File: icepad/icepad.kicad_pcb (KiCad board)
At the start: 2 copper layers, 50 parts, among them U1 STM32F042K6Tx, U2 TPD2EUSB30A, U3 IES0105S03

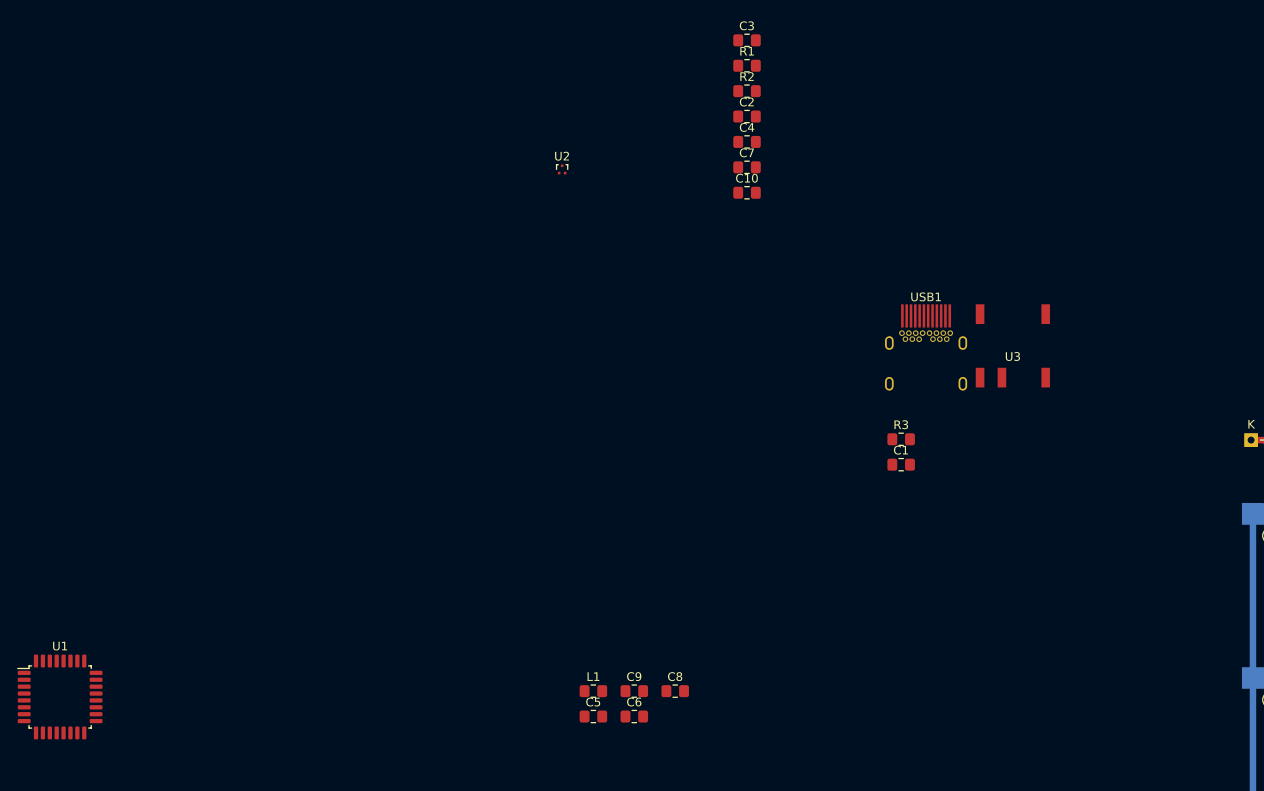
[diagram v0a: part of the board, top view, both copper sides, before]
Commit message: routed MCU and connector
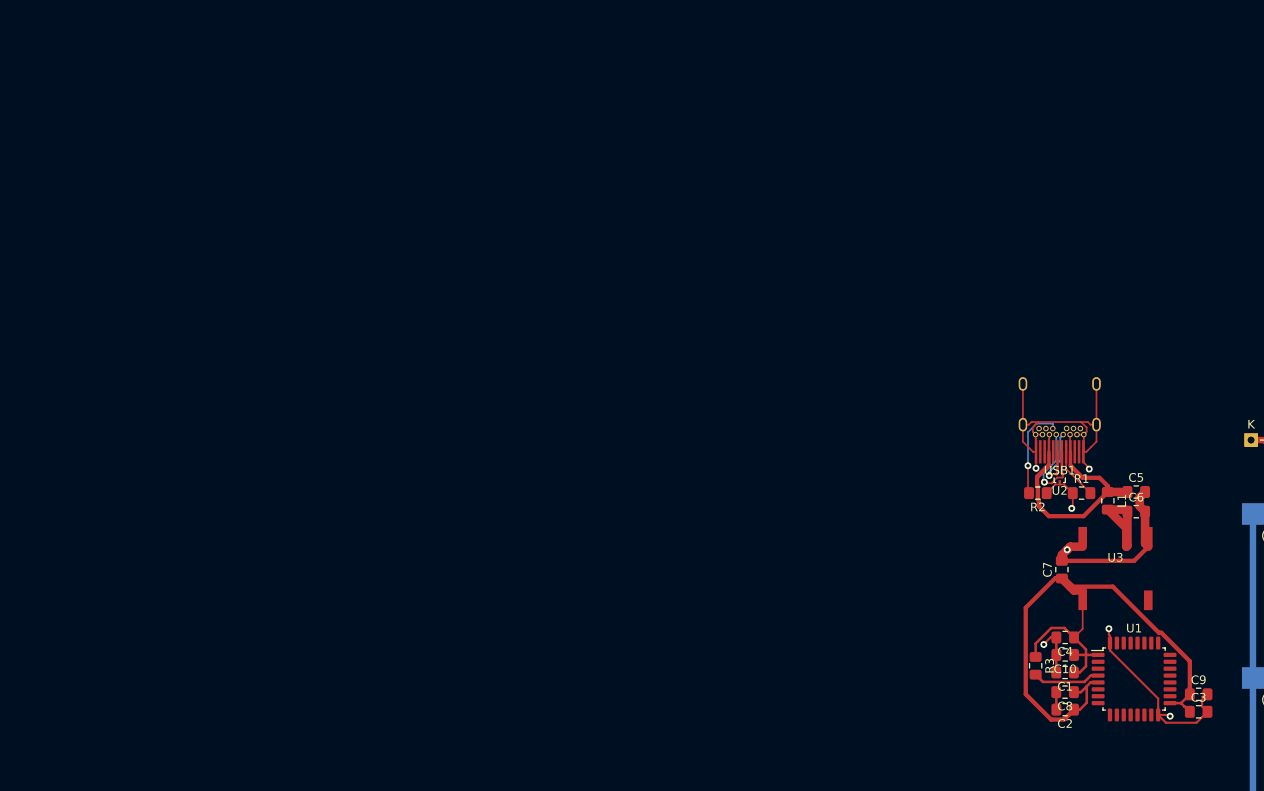
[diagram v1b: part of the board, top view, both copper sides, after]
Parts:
- moved U1 124.7 mm to (155.3, 89.7)
- moved C3 94.0 mm to (162.8, 93.5)
- moved C2 78.2 mm to (147.3, 93.2), turned to 180 degrees
- moved C4 68.4 mm to (147.3, 84.8), turned to 180 degrees
- moved C5 68.2 mm to (155.6, 67.9)
- moved U2 68.0 mm to (146.7, 66.3), turned to 180 degrees
- moved C9 65.5 mm to (162.8, 91.4)
- moved C10 65.2 mm to (147.3, 86.9), turned to 180 degrees
- moved L1 63.7 mm to (152.3, 69.0), turned to 270 degrees
- moved R1 63.0 mm to (149.2, 68.1)
- moved C6 63.0 mm to (155.6, 70.2)
- moved C7 59.3 mm to (146.9, 77.0), turned to 90 degrees
- moved R2 57.6 mm to (144.1, 68.1), turned to 180 degrees
- moved C8 45.3 mm to (147.3, 91.2), turned to 180 degrees
- moved C1 30.7 mm to (147.3, 88.9), turned to 180 degrees
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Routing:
- net GND: track 0.00 -> 98.0 mm, vias 0 -> 7
- net +3V3: track 0.00 -> 79.9 mm
- net VBUS: track 0.00 -> 30.6 mm
- net DP: track 0.00 -> 11.9 mm, vias 0 -> 1
- net Net-(C6-Pad1): track 0.00 -> 11.7 mm
- net Net-(R2-Pad2): track 0.00 -> 11.0 mm, vias 0 -> 1
- net DN: track 0.00 -> 9.05 mm, vias 0 -> 1
- net Net-(R3-Pad2): track 0.00 -> 7.91 mm
- net Net-(R1-Pad2): track 0.00 -> 5.97 mm
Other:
- net class Default: clearance 0.25 -> 0.2; trace_width 0.75 -> 0.5
- net class Key Matrix added: clearance 0.2, trace_width 0.75, via_dia 0.8, via_drill 0.4
- rule trace_clearance: 0.25 -> 0.2

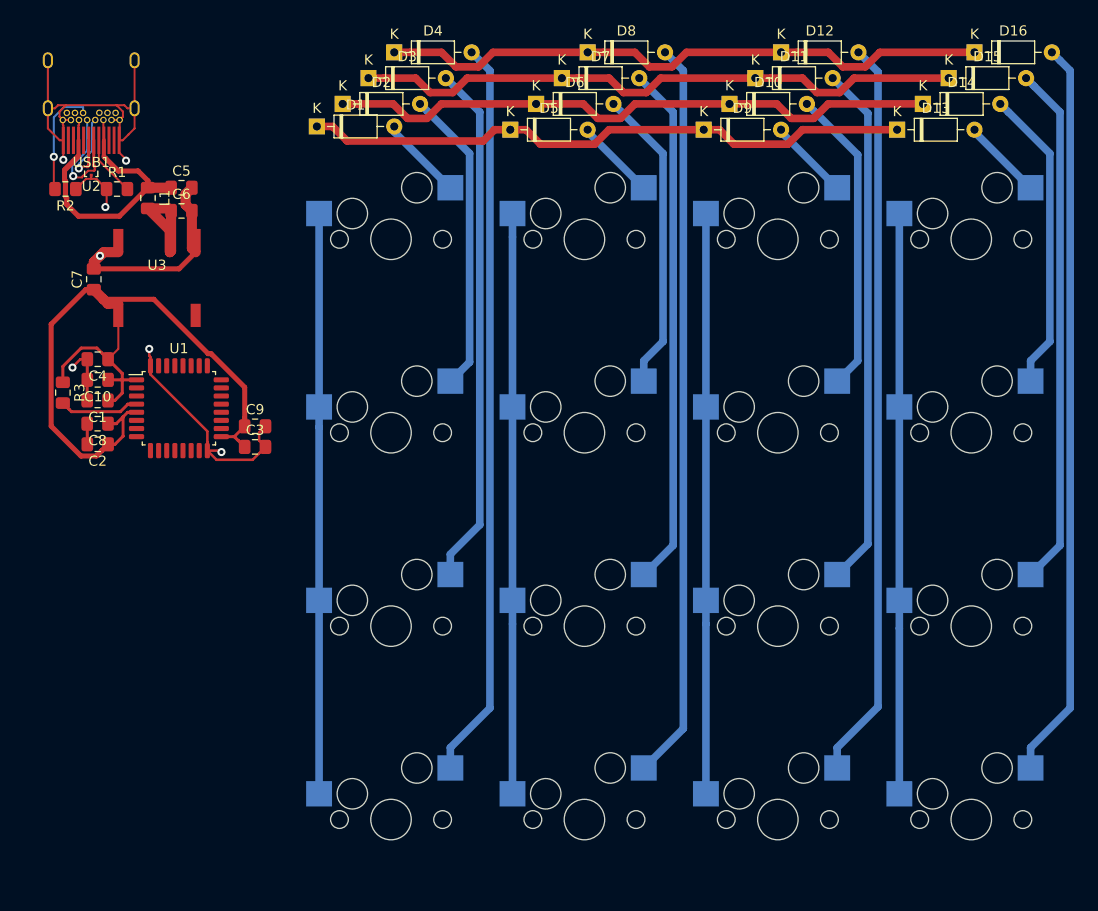
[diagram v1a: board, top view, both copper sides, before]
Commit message: completed routing without led
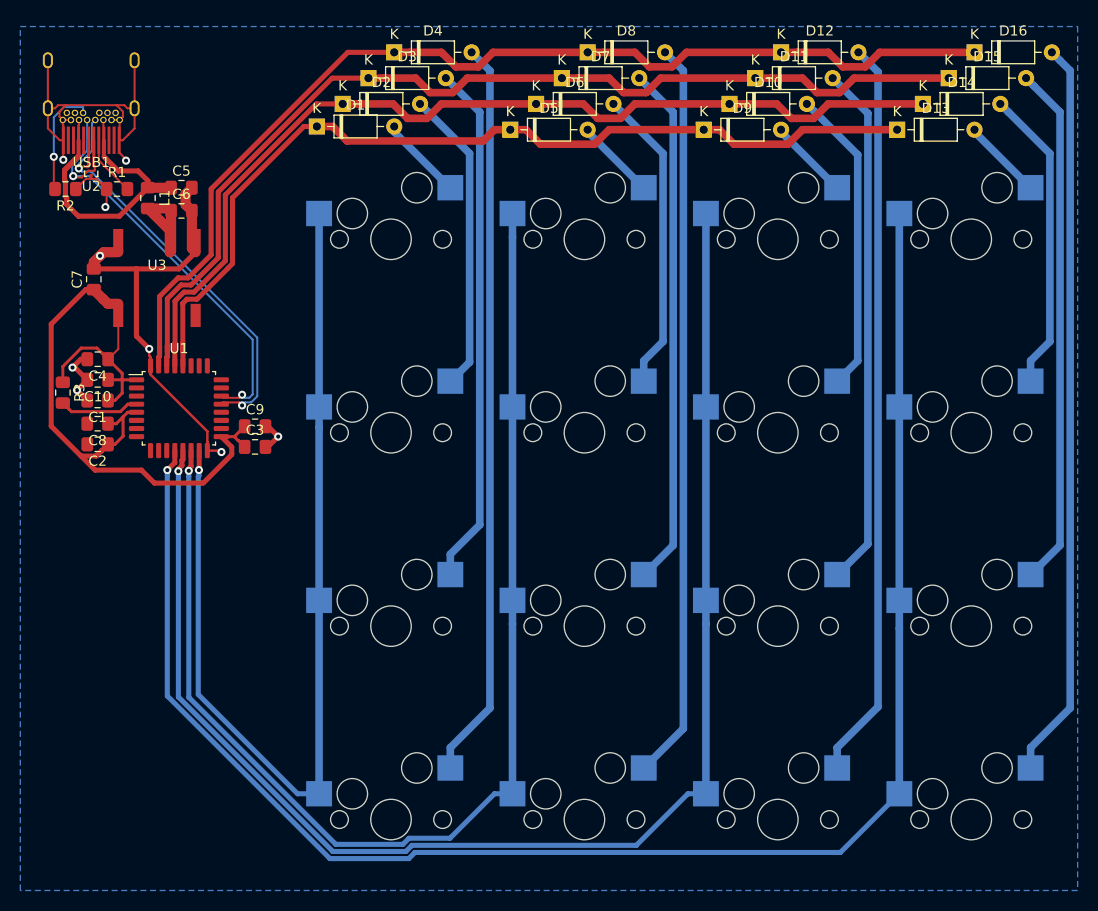
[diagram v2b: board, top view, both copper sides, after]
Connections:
- U1 pad 12: Net-(U1-Pad12) -> Col_3_Key
- U1 pad 13: Net-(U1-Pad13) -> Col_2_Key
- U1 pad 14: Net-(U1-Pad14) -> Col_1_Key
- U1 pad 15: Net-(U1-Pad15) -> Col_0_Key
- U1 pad 21: Net-(U1-Pad21) -> DN
- U1 pad 22: Net-(U1-Pad22) -> DP
- U1 pad 28: Net-(U1-Pad28) -> Row_0_Key
- U1 pad 29: Net-(U1-Pad29) -> Row_1_Key
- U1 pad 30: Net-(U1-Pad30) -> Row_2_Key
- U1 pad 31: Net-(U1-Pad31) -> Row_3_Key
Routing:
- net Col_3_Key: track 57.2 -> 163.0 mm, vias 0 -> 1
- net Col_2_Key: track 57.2 -> 142.2 mm, vias 0 -> 1
- net Col_1_Key: track 57.2 -> 121.5 mm, vias 0 -> 1
- net Row_3_Key: track 60.7 -> 104.4 mm
- net Col_0_Key: track 57.2 -> 98.9 mm, vias 0 -> 1
- net Row_2_Key: track 60.7 -> 100.4 mm
- net Row_1_Key: track 60.7 -> 96.3 mm
- net DN: track 9.05 -> 43.4 mm, vias 1 -> 2
- net DP: track 11.9 -> 45.2 mm, vias 1 -> 2
- net Row_0_Key: track 60.6 -> 91.7 mm
- net +3V3: track 79.9 -> 77.9 mm
- net GND: track 98.0 -> 99.6 mm, vias 7 -> 9
- added copper zone on B.Cu, net GND

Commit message: added jlcpcb stock and new pcb design
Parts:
- removed C10: 4.7uF, Capacitor_SMD:C_0805_2012Metric_Pad1.15x1.40mm_HandSolder
- added J1: Conn_01x04, Connector_PinHeader_2.54mm:PinHeader_1x04_P2.54mm_Horizontal, F.Cu at (413.7, 71.8)
- added R4: 453k, Resistor_SMD:R_0805_2012Metric, F.Cu at (298.4, 105.4)
- added R5: 100k, Resistor_SMD:R_0805_2012Metric, F.Cu at (298.4, 110.5)
- C5: value 4.7uF -> 1uF
- C7: value 10uF -> 4.7uF
- C8: value 1uF -> 4.7uF
- C9: value 4.7uF -> 10uF
- D1, D10, D11, D12, D13, D14, D15, D16, D2, D3, D4, D5, D6, D7, D8, D9: value D_Small -> 1N4148WS; footprint Diode_THT:D_DO-35_SOD27_P7.62mm_Horizontal -> Diode_SMD:D_SOD-323
- L1: value 6.8uH -> 2.2uH; footprint Inductor_SMD:L_0805_2012Metric_Pad1.15x1.40mm_HandSolder -> Inductor_SMD:L_0805_2012Metric
- MX1, MX10, MX11, MX12, MX13, MX14, MX15, MX16, MX2, MX3, MX4, MX5, MX6, MX7, MX8, MX9: footprint MX_Only:MXOnly-1U-Hotswap -> MX_Only:MXOnly-1U
- U2: value TPD2EUSB30A -> USBLC6-2SC6; footprint Package_TO_SOT_SMD:Texas_DRT-3 -> Package_TO_SOT_SMD:SOT-23-6
- U3: value IES0105S03 -> TLV62568DRL; footprint IES0105S03:IES0105S03 -> Package_TO_SOT_SMD:SOT-563
- moved USB1 261.3 mm to (406.1, 82.7), turned to 0 degrees
- moved U1 251.3 mm to (406.6, 89.9)
- moved U3 196.2 mm to (353.1, 81.3), turned to 0 degrees
- moved U2 191.2 mm to (337.8, 72.4), turned to 0 degrees
- moved L1 189.2 mm to (336.9, 110.5), turned to 0 degrees
- moved C7 173.6 mm to (315.0, 120.7), turned to 0 degrees
- moved C8 171.2 mm to (315.0, 125.7), turned to 0 degrees
- moved C4 168.9 mm to (315.0, 105.4), turned to 0 degrees
- moved C1 167.7 mm to (315.0, 90.2), turned to 0 degrees
- moved C2 167.7 mm to (315.0, 95.2), turned to 0 degrees
- moved C6 165.7 mm to (315.0, 115.6)
- moved C5 165.0 mm to (315.0, 110.5)
- moved C9 157.1 mm to (315.0, 130.8)
- moved R2 156.7 mm to (298.4, 95.2), turned to 0 degrees
- moved R3 155.0 mm to (298.4, 100.3), turned to 0 degrees
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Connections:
- C5 pad 1: VBUS -> +3V3
- C6 pad 1: Net-(C6-Pad1) -> +3V3
- C8 pad 1: +3V3 -> VBUS
- L1 pad 1: VBUS -> Net-(L1-Pad1)
- L1 pad 2: Net-(C6-Pad1) -> +3V3
- R3 pad 1: +3V3 -> Net-(R3-Pad1)
- R3 pad 2: Net-(R3-Pad2) -> +3V3
- U1 pad 10: Net-(U1-Pad10) -> (no net)
- U1 pad 11: Net-(U1-Pad11) -> (no net)
- U1 pad 18: Net-(U1-Pad18) -> (no net)
- U1 pad 19: Net-(U1-Pad19) -> (no net)
- U1 pad 2: Net-(U1-Pad2) -> (no net)
- U1 pad 20: Net-(U1-Pad20) -> (no net)
- U1 pad 23: Net-(U1-Pad23) -> SWDIO
- U1 pad 24: Net-(U1-Pad24) -> SWCLK
- U1 pad 25: Net-(U1-Pad25) -> (no net)
- U1 pad 26: Net-(U1-Pad26) -> (no net)
- U1 pad 27: Net-(U1-Pad27) -> (no net)
- U1 pad 3: Net-(U1-Pad3) -> (no net)
- U1 pad 4: Net-(R3-Pad2) -> Net-(R3-Pad1)
- U1 pad 6: Net-(U1-Pad6) -> (no net)
- U1 pad 7: Net-(U1-Pad7) -> (no net)
- U1 pad 8: Net-(U1-Pad8) -> (no net)
- U1 pad 9: Net-(U1-Pad9) -> (no net)
- U2 pad 2: DN -> GND
- U2 pad 3: GND -> DN
- U3 pad 1: GND -> Net-(R4-Pad2)
- U3 pad 2: Net-(C6-Pad1) -> GND
- U3 pad 4: GND -> Net-(L1-Pad1)
- U3 pad 5: +3V3 -> VBUS
- USB1 pad 10: Net-(USB1-Pad10) -> (no net)
- USB1 pad 11: Net-(USB1-Pad11) -> (no net)
- USB1 pad 14: Net-(USB1-Pad14) -> (no net)
- USB1 pad 15: Net-(USB1-Pad15) -> (no net)
- USB1 pad 2: Net-(USB1-Pad2) -> (no net)
- USB1 pad 20: Net-(USB1-Pad20) -> (no net)
- USB1 pad 22: Net-(USB1-Pad22) -> (no net)
- USB1 pad 23: Net-(USB1-Pad23) -> (no net)
- USB1 pad 3: Net-(USB1-Pad3) -> (no net)
- USB1 pad 8: Net-(USB1-Pad8) -> (no net)
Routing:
- net GND: track 99.6 -> 0.00 mm, vias 9 -> 0
- net Col_3_Key: track 163.0 -> 66.4 mm, vias 1 -> 0
- net +3V3: track 77.9 -> 0.00 mm
- net Col_2_Key: track 142.2 -> 66.4 mm, vias 1 -> 0
- net Row_3_LED: track 0.00 -> 60.6 mm
- net Row_1_LED: track 0.00 -> 60.6 mm
- net Row_0_LED: track 0.00 -> 60.6 mm
- net Row_2_LED: track 0.00 -> 60.6 mm
- net Col_3_LED: track 0.00 -> 60.1 mm
- net Col_2_LED: track 0.00 -> 60.1 mm
- net Col_1_LED: track 0.00 -> 60.1 mm
- net Col_0_LED: track 0.00 -> 60.1 mm
- net Col_1_Key: track 121.5 -> 66.4 mm, vias 1 -> 0
- net DP: track 45.2 -> 0.00 mm, vias 2 -> 0
- net DN: track 43.4 -> 0.00 mm, vias 2 -> 0
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- removed copper zone on B.Cu, net GND
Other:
- board outline added: 100 x 100 mm

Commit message: complete new pcba design
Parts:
- removed R2: 5k1, Resistor_SMD:R_0805_2012Metric_Pad1.15x1.40mm_HandSolder
- removed USB1: Wurth-632723300011, Type-C:Wurth-632723300011-HandSoldering
- added C10: 100nF, Capacitor_SMD:C_0805_2012Metric, F.Cu at (84.0, 58.0)
- added J2: USB_B_Mini, digikey-footprints:USB_Mini_B_Female_548190519, F.Cu at (91.0, 59.2)
- added MNT: MountingHole_2.2mm_M2, MountingHole:MountingHole_2.2mm_M2, F.Cu at (177.0, 147.0)
- added MNT: MountingHole_2.2mm_M2, MountingHole:MountingHole_2.2mm_M2, F.Cu at (83.0, 147.0)
- added MNT: MountingHole_2.2mm_M2, MountingHole:MountingHole_2.2mm_M2, F.Cu at (177.0, 53.0)
- added MNT: MountingHole_2.2mm_M2, MountingHole:MountingHole_2.2mm_M2, F.Cu at (83.0, 53.0)
- C1, C2, C3, C4, C5, C6, C7, C8, C9: footprint Capacitor_SMD:C_0805_2012Metric_Pad1.15x1.40mm_HandSolder -> Capacitor_SMD:C_0805_2012Metric
- R1: value 5k1 -> 330; footprint Resistor_SMD:R_0805_2012Metric_Pad1.15x1.40mm_HandSolder -> Resistor_SMD:R_0805_2012Metric
- R3: footprint Resistor_SMD:R_0805_2012Metric_Pad1.15x1.40mm_HandSolder -> Resistor_SMD:R_0805_2012Metric
- moved J1 330.5 mm to (83.6, 86.1), turned to 180 degrees
- moved U1 314.9 mm to (91.7, 91.2), turned to 90 degrees
- moved U3 267.5 mm to (85.9, 69.2), turned to 270 degrees
- moved L1 256.8 mm to (83.1, 71.6), turned to 270 degrees
- moved U2 247.0 mm to (91.0, 63.9), turned to 90 degrees
- moved C8 236.8 mm to (85.9, 66.0)
- moved C9 236.4 mm to (85.9, 72.6)
- moved C7 228.1 mm to (87.6, 101.6), turned to 180 degrees
- moved C1 227.4 mm to (87.6, 97.5), turned to 180 degrees
- moved C4 227.4 mm to (87.6, 99.6), turned to 180 degrees
- moved C5 222.0 mm to (93.2, 99.6)
- moved C2 221.8 mm to (93.2, 97.5)
- moved C6 221.6 mm to (95.5, 84.8)
- moved C3 220.2 mm to (95.5, 82.5)
- moved R1 216.6 mm to (84.0, 60.0), turned to 180 degrees
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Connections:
- R1 pad 1: GND -> Net-(C10-Pad2)
- R1 pad 2: Net-(R1-Pad2) -> GND
- U1 pad 12: Col_3_Key -> (no net)
- U1 pad 13: Col_2_Key -> (no net)
- U1 pad 14: Col_1_Key -> (no net)
- U1 pad 15: Col_0_Key -> (no net)
- U1 pad 28: Row_0_Key -> (no net)
- U1 pad 29: Row_1_Key -> (no net)
- U1 pad 30: Row_2_Key -> (no net)
- U1 pad 31: Row_3_Key -> (no net)
- U2 pad 4: DN -> DN_pre
- U2 pad 6: DP -> DP_pre
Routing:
- net Col_3_Key: track 66.4 -> 135.5 mm
- net Col_2_Key: track 66.4 -> 115.6 mm
- net +3V3: track 0.00 -> 43.4 mm, vias 0 -> 2
- net Col_1_Key: track 66.4 -> 95.8 mm
- net DP: track 0.00 -> 25.2 mm
- net DN: track 0.00 -> 22.3 mm
- net GND: track 0.00 -> 19.5 mm, vias 0 -> 1
- net Row_3_Key: track 78.3 -> 96.8 mm
- net VBUS: track 0.00 -> 17.8 mm
- net Row_2_LED: track 60.6 -> 78.3 mm
- net Row_1_LED: track 60.6 -> 78.3 mm
- net Row_3_LED: track 60.6 -> 77.9 mm
- net Row_0_LED: track 60.6 -> 77.7 mm
- net Net-(C10-Pad2): track 0.00 -> 14.8 mm
- net Row_2_Key: track 73.3 -> 87.9 mm
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- added copper zone on F.Cu, net +3V3
- added copper zone on B.Cu, net GND
- added copper zone on F.Cu, net GND
- added copper zone on F.Cu, net Net-(L1-Pad1)
